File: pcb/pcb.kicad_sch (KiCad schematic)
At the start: 13 parts, among them J1 USB_C_Receptacle_PowerOnly_6P, U1 BQ24075RGTR

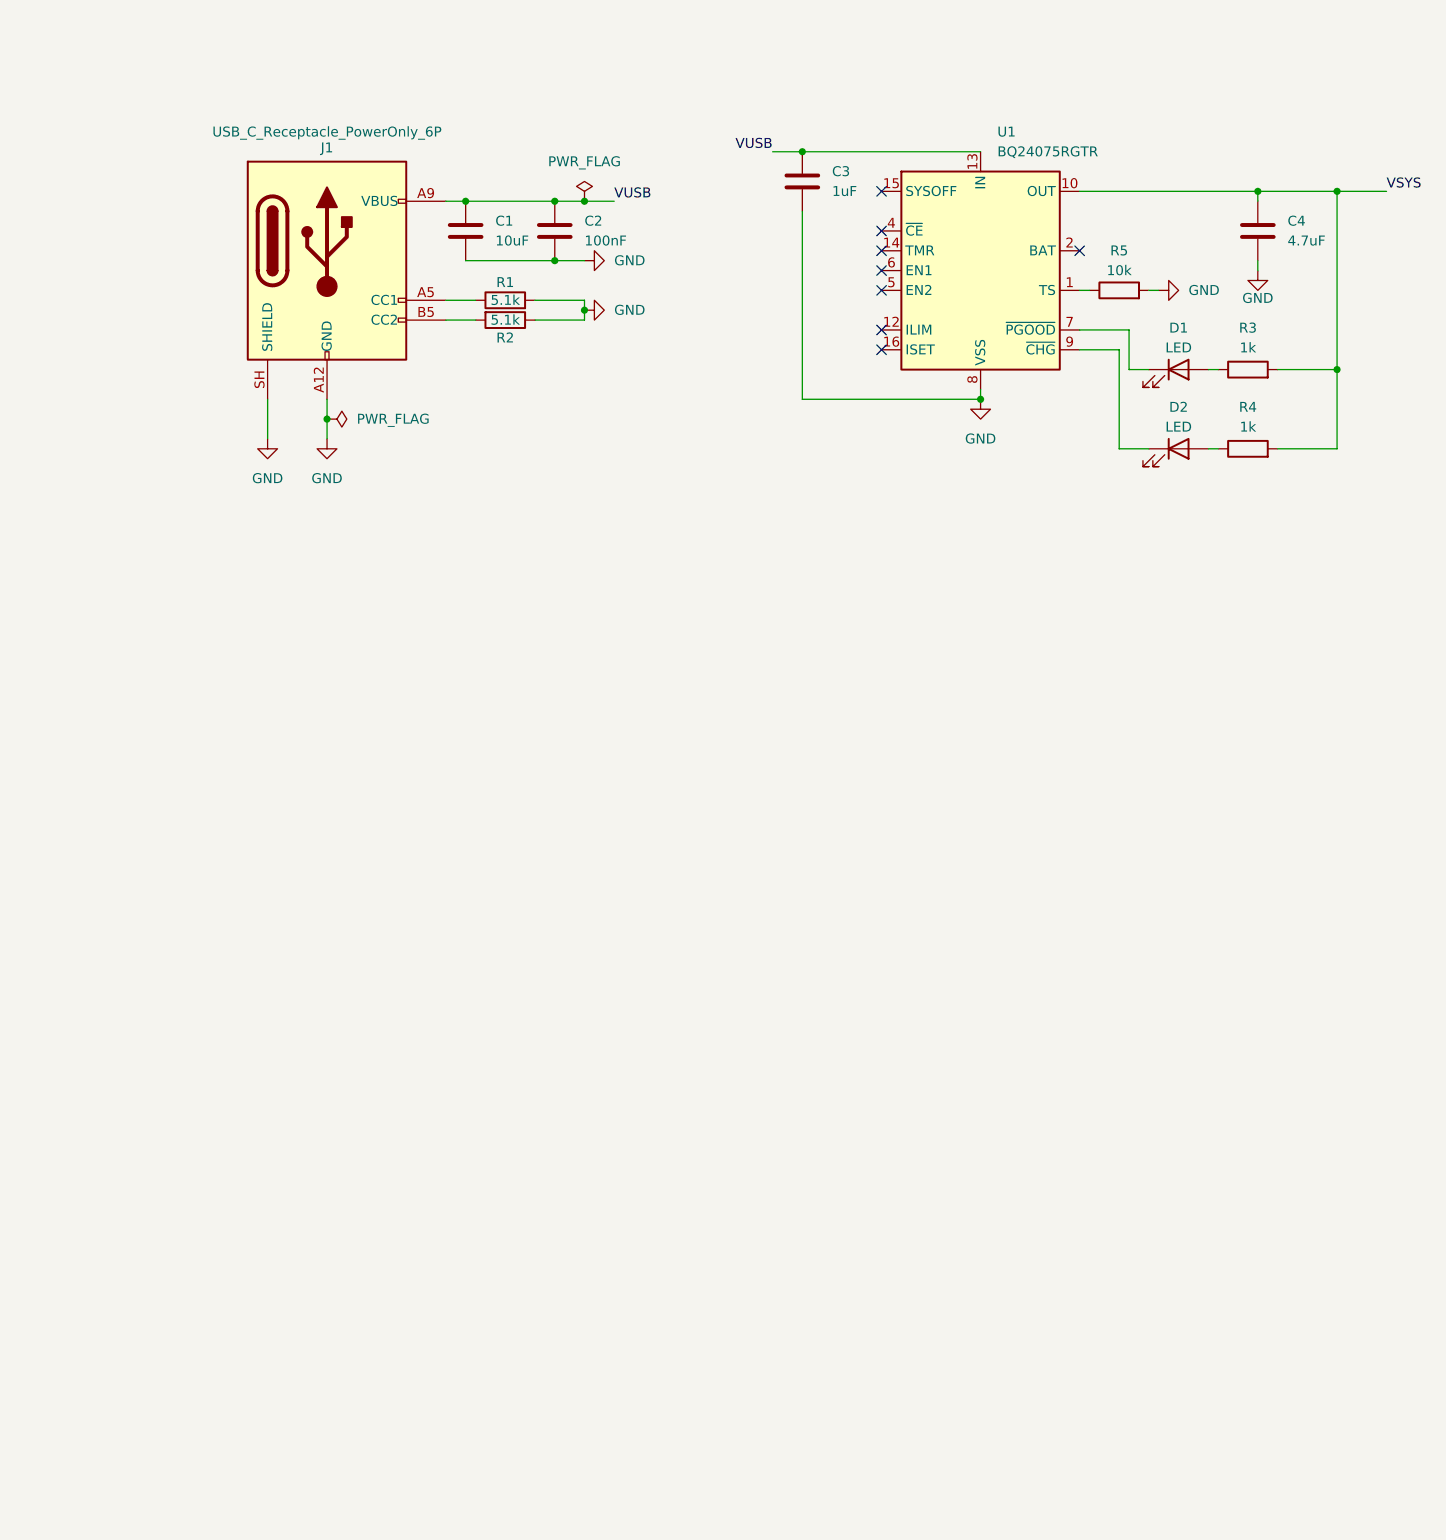
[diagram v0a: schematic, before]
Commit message: Added SamacSys library (Mouser LibraryLoader) and almost finished the power section
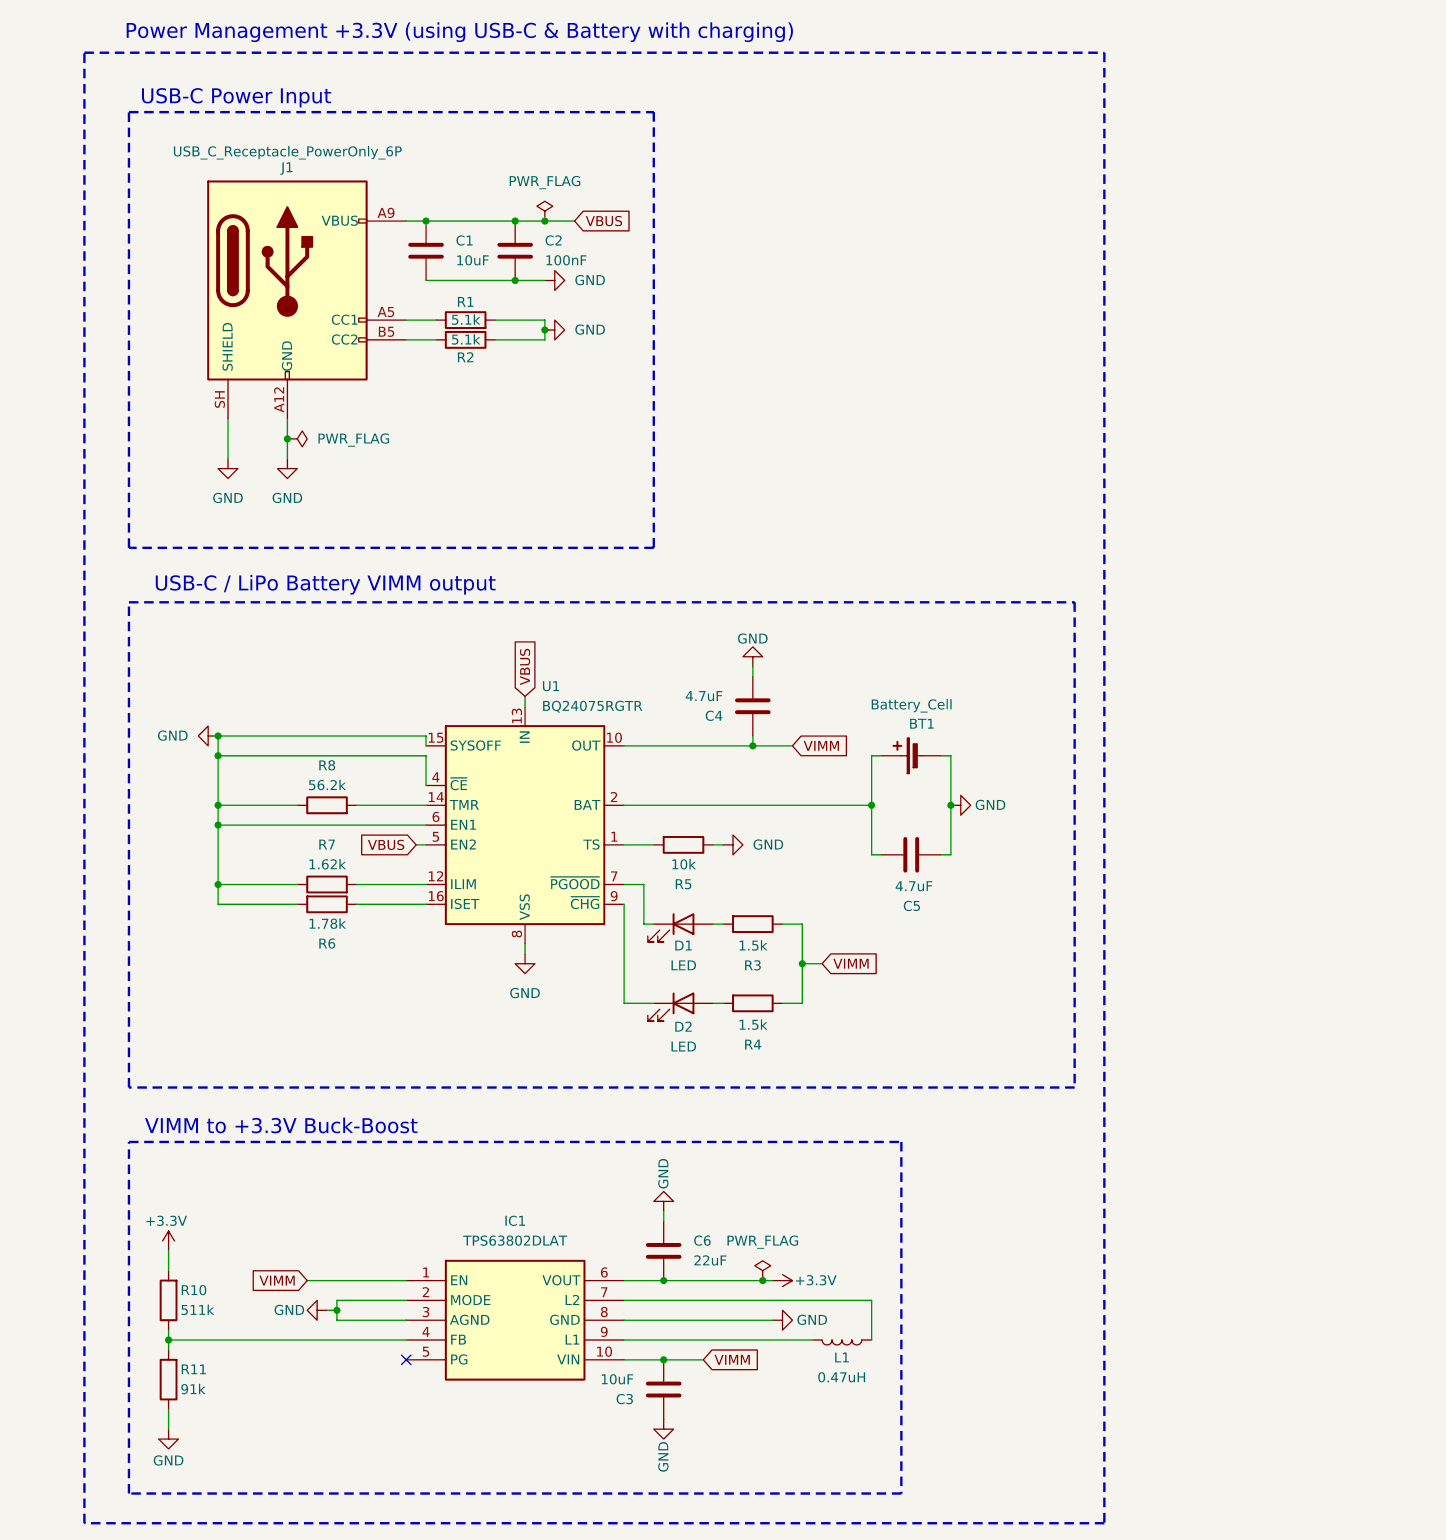
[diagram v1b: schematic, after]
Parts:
- added BT1: Battery_Cell, Connector_JST:JST_PH_B2B-PH-K_1x02_P2.00mm_Vertical, symbol Device:Battery_Cell
- added C5: 4.7uF, symbol Device:C
- added C6: 22uF, symbol Device:C
- added IC1: TPS63802DLAT, SamacSys:TPS63802DLAT, symbol SamacSys:TPS63802DLAT
- added L1: 0.47uH, symbol Device:L
- added R10: 511k, symbol Device:R
- added R11: 91k, symbol Device:R
- added R6: 1.78k, symbol Device:R
- added R7: 1.62k, symbol Device:R
- added R8: 56.2k, symbol Device:R
- C3: value 1uF -> 10uF; footprint Package_DFN_QFN:VQFN-16-1EP_3x3mm_P0.5mm_EP1.6x1.6mm -> (none)
- D1, D2: footprint Transformer_SMD:Transformer_ED8_4-Lead_10.5x8mm_P5mm -> (none)
- J1: Distributor Link 1 (none) -> https://www.mouser.de/en/ProductDetail/GCT/USB4970-00-A?qs=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
- R3, R4: value 1k -> 1.5k
- U1: Distributor Link 1 (none) -> https://www.mouser.de/en/ProductDetail/Texas-Instruments/BQ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
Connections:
- net GND: now also C3.1, R5.1, U1.15 (SYSOFF), U1.4 (~{CE}), U1.6 (EN1), BT1.2 (-), C5.2, C6.1, IC1.2 (MODE), IC1.3 (AGND), IC1.8 (GND), R11.1, R6.2, R7.1, R8.1; no longer C3.2, R5.2
- net at D1.2 (A): now also R3.2; no longer R3.1
- net at D2.2 (A): now also R4.2; no longer R4.1
- net at U1.1 (TS): now also R5.2; no longer R5.1
- net at U1.12 (ILIM): now also R7.2
- net at U1.14 (TMR): now also R8.2
- net at U1.16 (ISET): now also R6.1
- net at U1.2 (BAT), U1.3 (BAT): now also BT1.1 (+), C5.1
- net VBUS: now reaches U1.5 (EN2)
- net VBUS: now also C1.2, C2.2, J1.A9 (VBUS), J1.B9 (VBUS), U1.13 (IN)
- net VSYS renamed VIMM
- net VIMM: now also C3.2, R3.1, R4.1, IC1.1 (EN), IC1.10 (VIN); no longer R3.2, R4.2
- removed net VUSB: C1.2, C2.2, C3.1, J1.A9 (VBUS), J1.B9 (VBUS), U1.13 (IN)
- new net: IC1.7 (L2), L1.1
- new net: IC1.9 (L1), L1.2
- new net: IC1.4 (FB), R10.1, R11.2
- new net +3.3V: C6.2, IC1.6 (VOUT), R10.2
- no-connect marks 8 -> 1
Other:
- note added: "Power Management +3.3V (using USB-C & Battery with charging)"
- note added: "USB-C / LiPo Battery VIMM output"
- note added: "USB-C Power Input"
- note added: "VIMM to +3.3V Buck-Boost"
- moved on the sheet: C1, C2, C4, D1, D2, J1, R1, R2, R3, R4, R5, U1

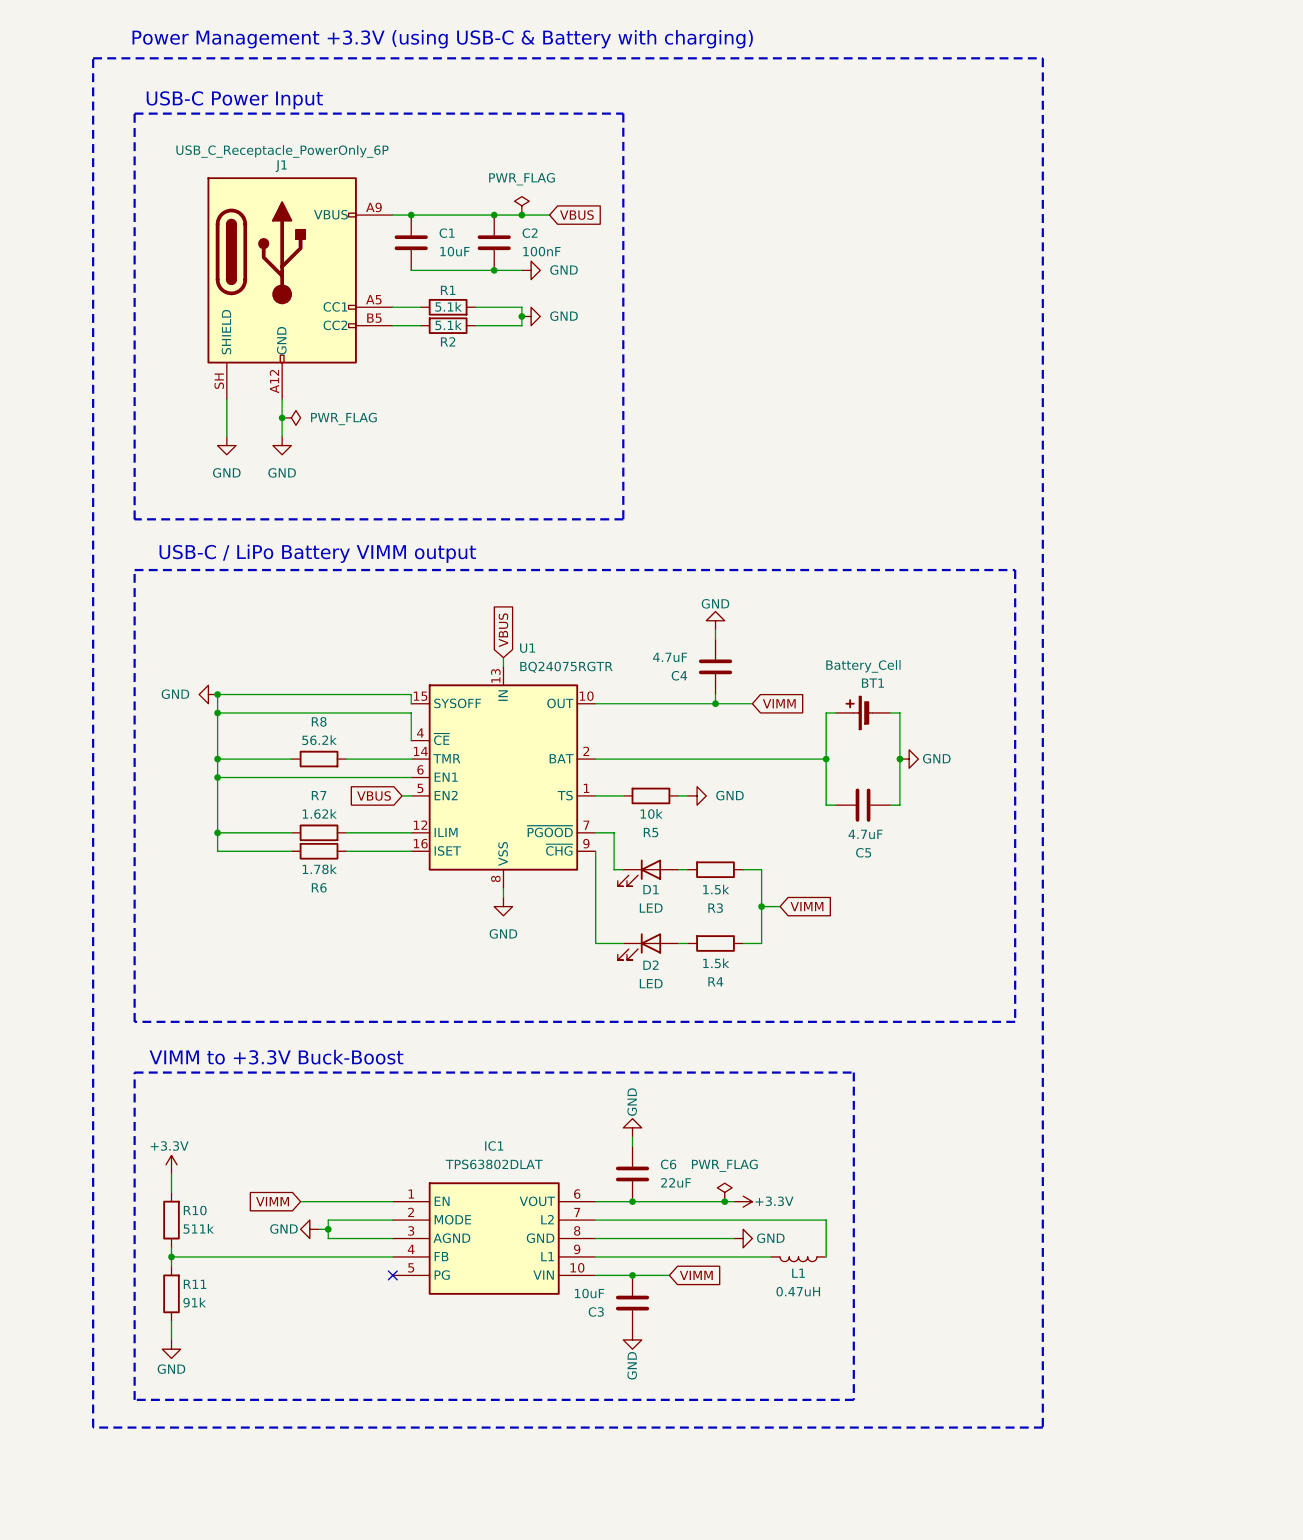
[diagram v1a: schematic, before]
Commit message: Added USB-C CC detection/selection to the schematic
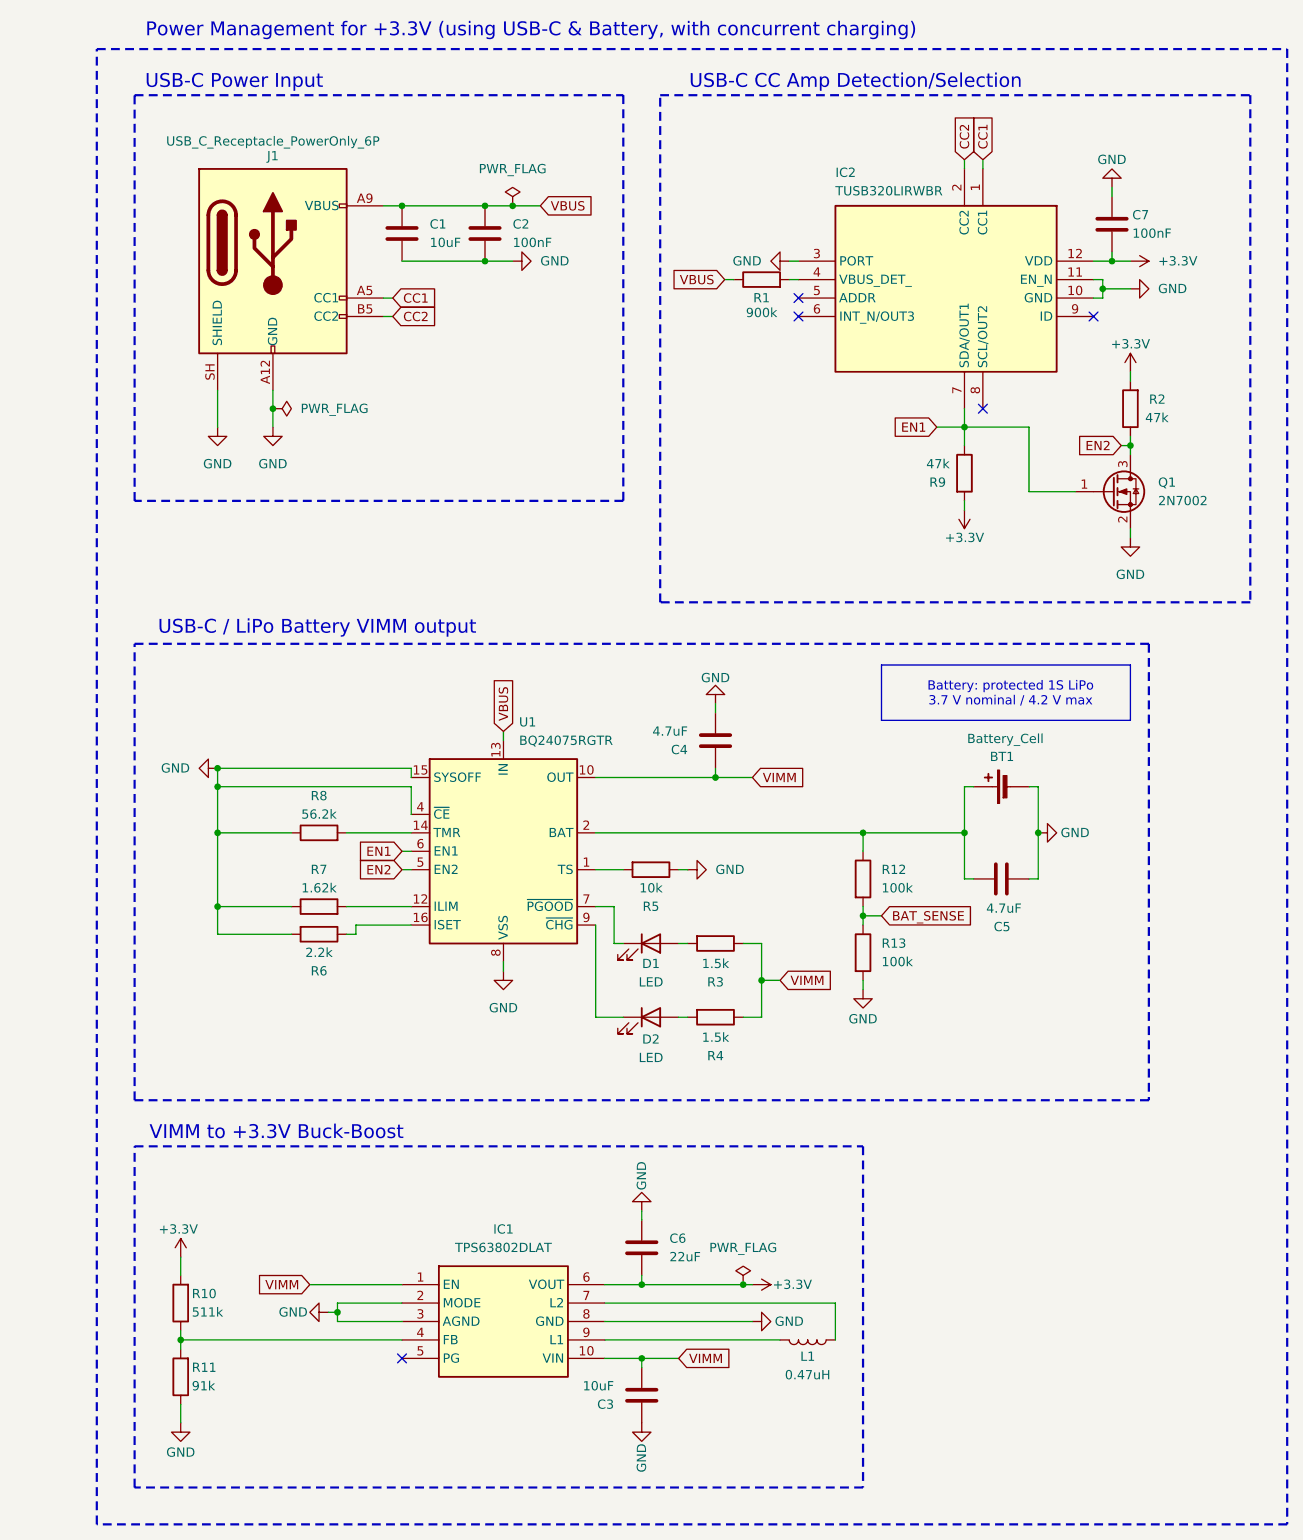
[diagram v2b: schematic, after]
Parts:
- added C7: 100nF, symbol Device:C
- added IC2: TUSB320LIRWBR, SamacSys:TUSB320LIRWBR, symbol SamacSys:TUSB320LIRWBR
- added Q1: 2N7002, symbol Transistor_FET:2N7002
- added R12, R13: 100k, symbol Device:R
- added R9: 47k, symbol Device:R
- R1: value 5.1k -> 900k
- R2: value 5.1k -> 47k
- R6: value 1.78k -> 2.2k
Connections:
- net +3.3V: now also R2.2, C7.2, IC2.12 (VDD), R9.2
- net GND: now also C7.1, IC2.10 (GND), IC2.11 (EN_N), IC2.3 (PORT), Q1.2 (S), R13.2; no longer R1.2, R2.1, U1.6 (EN1)
- net VBUS: now also R1.1; no longer U1.5 (EN2)
- net at BT1.1 (+), C5.1, U1.2 (BAT)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: now also R12.1
- net CC1: now reaches J1.A5 (CC1)
- net CC1: now also IC2.1 (CC1); no longer R1.1
- net CC2: now reaches J1.B5 (CC2)
- net CC2: now also IC2.2 (CC2); no longer R2.2
- new net: IC2.4 (VBUS_DET_), R1.2
- new net BAT_SENSE: R12.2, R13.1
- new net EN1: IC2.7 (SDA/OUT1), Q1.1 (G), R9.1, U1.6 (EN1)
- new net EN2: Q1.3 (D), R2.1, U1.5 (EN2)
- no-connect marks 1 -> 5
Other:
- note added: "Battery: protected 1S LiPo 3.7 V nominal / 4.2 V max"
- note added: "Power Management for +3.3V (using USB-C & Battery, with concurrent charging)"
- note added: "USB-C CC Amp Detection/Selection"
- note removed: "Power Management +3.3V (using USB-C & Battery with charging)"
- moved on the sheet: BT1, C1, C2, C3, C4, C5, C6, D1, D2, IC1, J1, L1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
